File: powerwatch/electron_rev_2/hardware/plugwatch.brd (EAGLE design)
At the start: 57.1 x 93 mm, 111 parts, among them J1 DM3AT-SF-PEJM5, J2 TC2030-JLINK-NL, SW4 SIP32510, U1 BGA725L6-ALT, U10 SIP32510, U11 SIP32510, U12 SIP32510, U2 SAFFB1G56KB0F0A, U3 ISL29035, U4 MAX-M8, U5 MAX740XESA, U6 MPU-9250, U7 NRF51822QF, U8 OPA322AIDBVT, U9 SIP32510, X1 ABS05-32.768KHZ-9-T, X2 16MHz

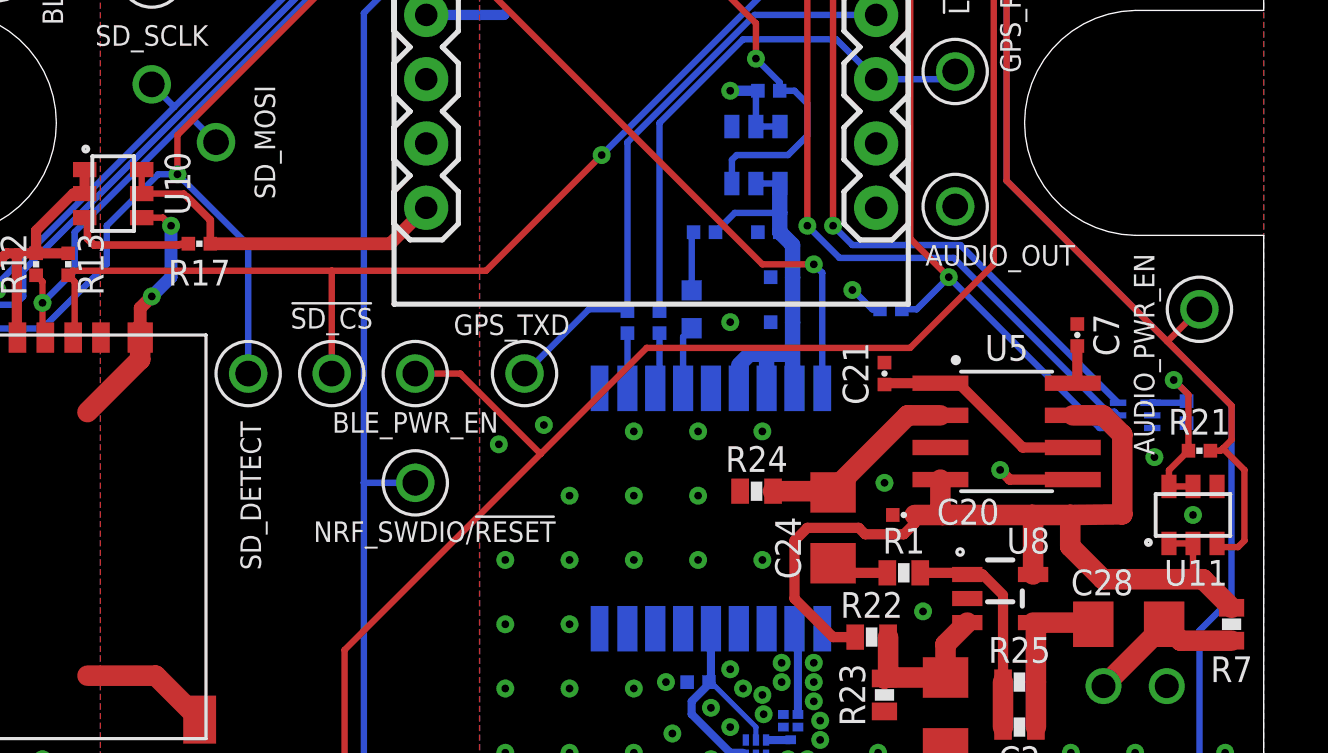
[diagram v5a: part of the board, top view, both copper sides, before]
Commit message: fixed up silk, renumber chips
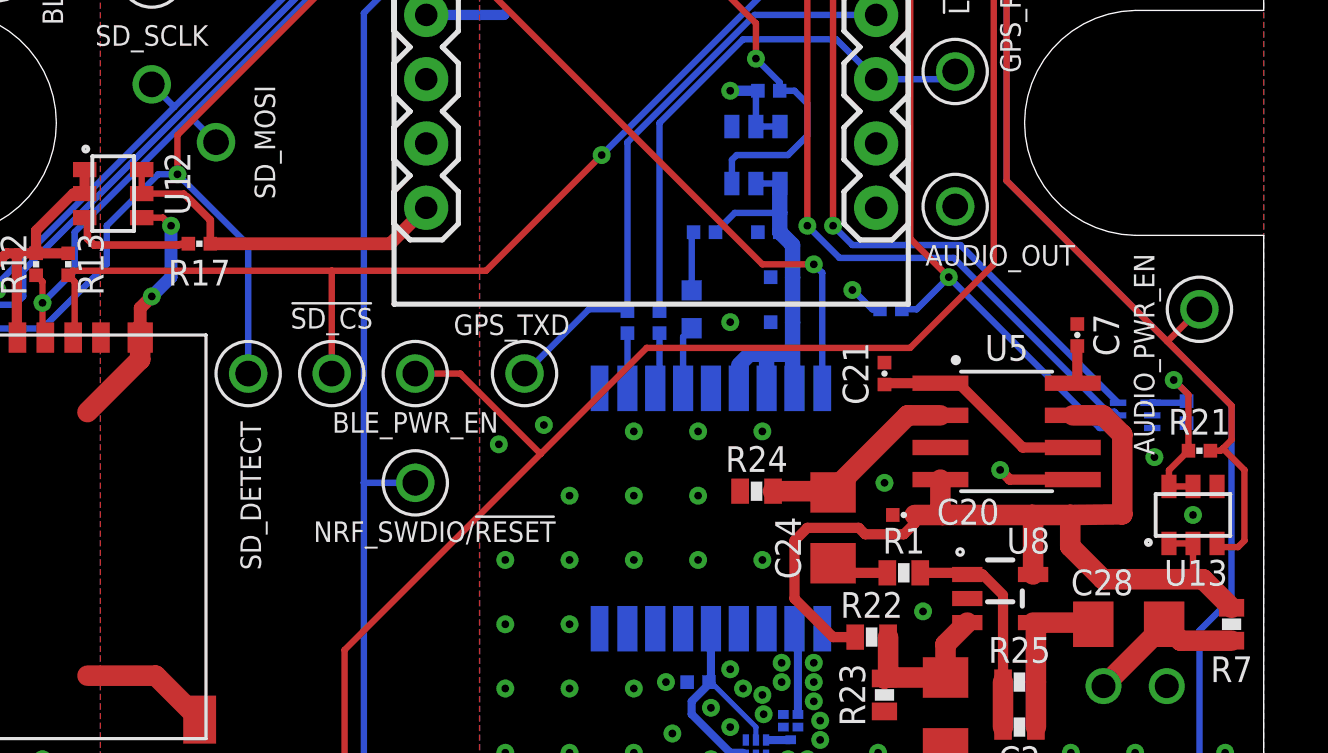
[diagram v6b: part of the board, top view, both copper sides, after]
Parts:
- removed SW4: SIP32510, chips:TSOT23-6
- added U13: SIP32510, chips:TSOT23-6
- L2: value 10uH -> 15nH; device passives:0603_CAP -> passives:0402_CAP
- L3: value 15nH -> 10uH; device passives:0402_CAP -> passives:0603_CAP
- moved U9 76.8 mm to (7.62, 84.3), turned to 0 degrees
- moved U11 42.1 mm to (18.8, 8.38), flipped to the bottom, turned to 180 degrees
- moved U10 25.4 mm to (37.1, 45.2), flipped to the bottom, turned to 0 degrees
- moved U12 25.4 mm to (11.7, 43.7), flipped to the top, turned to 270 degrees
- moved L2 1.30 mm to (19.0, 11.0), turned to 270 degrees
- moved L3 1.30 mm to (17.7, 11.3), turned to 90 degrees
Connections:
- net AUDIO_PWR_EN: now also U13.3; no longer U11.3
- net AVDD1: now also L2.1; no longer L3.1
- net BLE_PWR_EN: now also U11.3; no longer U9.3
- net DCC1: now also L3.2; no longer L2.2
- net GND: now also U13.4; no longer SW4.4
- net GPS_PWR_EN: now also U10.3; no longer U12.3
- net GPS_VCC: now also U10.1, U10.2; no longer U12.1, U12.2
- net N$14: now also U9.1, U9.2; no longer SW4.1, SW4.2
- net N$15: now also L2.2, L3.1; no longer L2.1, L3.2
- net N$18: now also U12.1, U12.2; no longer U10.1, U10.2
- net SD_ENABLE_POWER: now also U12.3; no longer U10.3
- net VCC: now also U13.5, U13.6; no longer SW4.5, SW4.6
- net VCC_A_MIC: now also U13.1, U13.2; no longer U11.1, U11.2
- net VCC_BLE: now also U11.1, U11.2; no longer U9.1, U9.2
- net WIFI_PWR_EN: now also U9.3; no longer SW4.3
